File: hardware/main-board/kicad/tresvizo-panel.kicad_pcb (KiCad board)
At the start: 4 copper layers, 82.8 x 79 mm, 137 parts, among them J101 PANEL_USB, J102 BATTERY, J301 GNSS, J401 TF-015, J402 BOTON, J403 OLED, J404 NTC, J405 IMU, J501 USB_C, J502 PANEL_USB, Q101 AO3400A, Q102 AO3401A, Q103 AO3400A, Q401 AO3401A, Q402 AO3400A, SW201 RESET, SW202 BOOT, U101 USBLC6-2SC6, U102 BQ25798RQMR, U103 MAX17048G+T10, U105 TPS62903RPJR, U201 ESP32-S3-WROOM-1-N16R2, U301 TPS63070RNMR, U302 USBLC6-2SC6, U303 USBLC6-2SC6, U501 USBLC6-2SC6

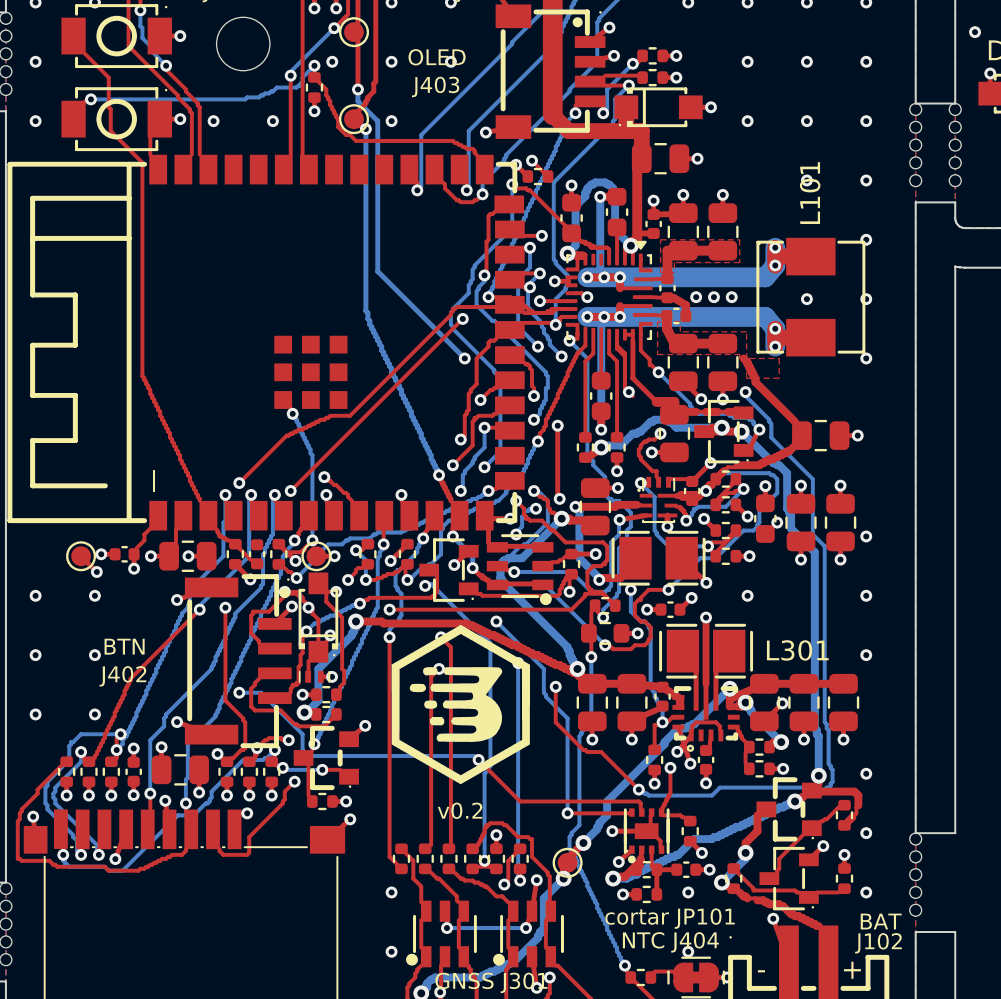
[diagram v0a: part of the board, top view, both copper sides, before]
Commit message: Placa principal v0.2: regulador de 3.3 V (TPS62903) colocado según su hoja de datos
- U105 y sus piezas pasan a la zona libre de la derecha de la placa.
- SW a L102 en 0.9 mm por F.Cu y sin vías. Antes daba un rodeo de 8.7 mm con dos vías y pasaba
  entre los pads de C115.
- C115, el 10 µF de entrada, queda a 0.4 mm de VIN y de GND, con EN saliendo entre sus pads.
- C118 y C119 (salida) junto a la salida de L102 y a GND; VOS toma la tensión en C118.
- FB con su divisor a 1.5 mm: 2.5 mm de pista sin vías (antes 8.6 mm con dos vías).
- Fuera los prerruteos de BUCK_SW y de la vía de GND de U105, que ya no hacen falta.
- ERC 0. DRC con 0 violaciones, 0 sin conectar y 0 de paridad en la placa, la panel-usb y el panel;
  128 de 128 conexiones; dos builds idénticos. Montaje en V2.3 sin choques nuevos.
- README: D+/D- con las cifras del ruteo actual (vienen de una revisión externa).
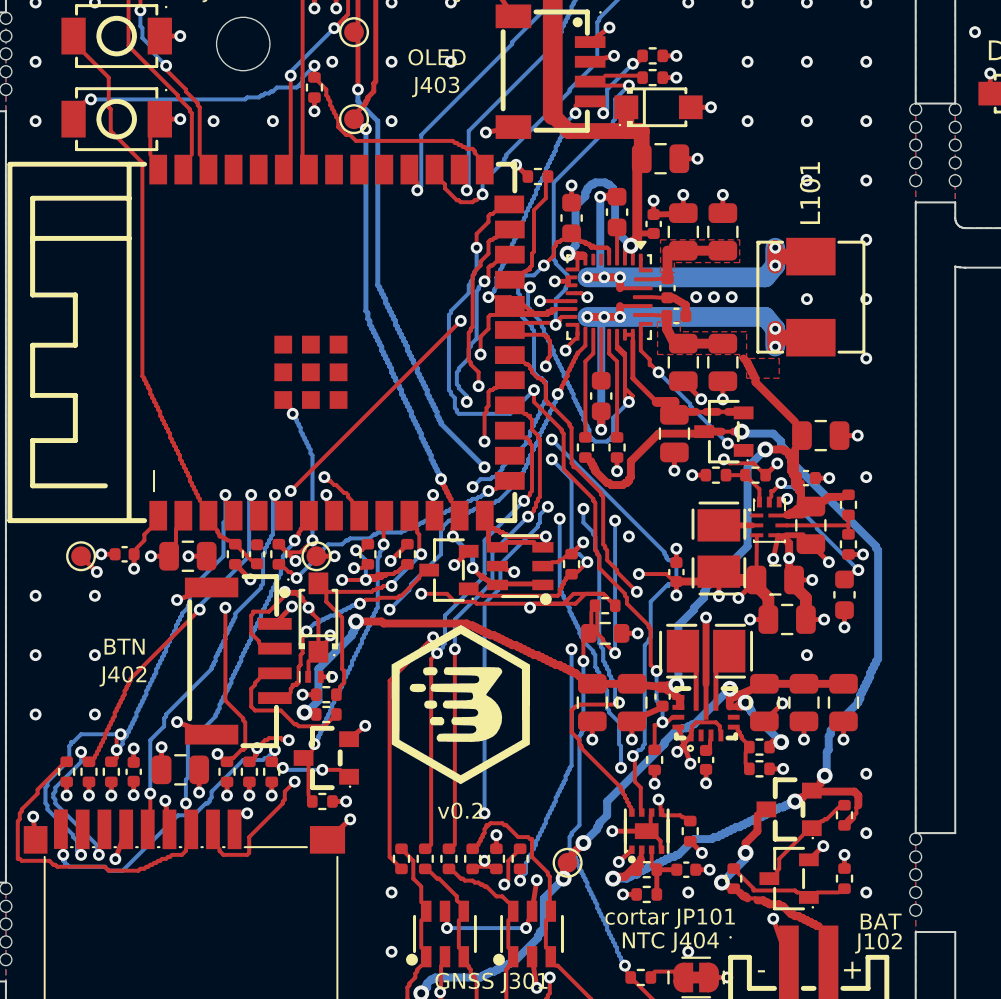
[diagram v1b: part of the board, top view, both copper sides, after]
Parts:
- moved C115 10.9 mm to (147.7, 140.9), turned to -90 degrees
- moved R116 6.51 mm to (149.6, 141.9), turned to -90 degrees
- moved R115 6.33 mm to (149.6, 139.9), turned to -90 degrees
- moved C116 5.79 mm to (147.4, 138.6), turned to 0 degrees
- moved U105 5.69 mm to (145.6, 140.6)
- moved C119 5.59 mm to (146.5, 145.7), turned to 0 degrees
- moved C117 5.55 mm to (149.4, 144.4), turned to -90 degrees
- moved R118 4.37 mm to (144.9, 138.4)
- moved C118 3.18 mm to (145.9, 143.7), turned to 0 degrees
- moved L102 3.09 mm to (143.1, 142.1), turned to -90 degrees
- moved R117 2.84 mm to (142.9, 138.4)
- moved C120 1.92 mm to (140.9, 143.3), turned to 90 degrees
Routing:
- net BTN_LED_EN: track 65.4 -> 25.6 mm, vias 5 -> 3
- net VSYS: track 91.1 -> 56.2 mm, vias 8 -> 4
- net I2C_SCL: track 77.8 -> 56.5 mm
- net GND: track 120.6 -> 130.6 mm, vias 155 -> 157
- net /Alimentación, carga y batería/BUCK_SW: track 8.68 -> 0.95 mm, vias 2 -> 0
- net /Alimentación, carga y batería/CHG_ILIM: track 22.7 -> 29.9 mm, vias 4 -> 5
- net /Alimentación, carga y batería/BUCK_FB: track 8.62 -> 2.47 mm, vias 2 -> 0
- net /Alimentación, carga y batería/REGN: track 53.3 -> 47.5 mm
- net /Alimentación, carga y batería/BUCK_EN: track 8.50 -> 4.13 mm, vias 2 -> 0
- net GNSS_PWR_EN: track 33.7 -> 38.0 mm
- net /Alimentación, carga y batería/BUCK_SS: track 11.4 -> 7.62 mm
- net +3V3: track 44.8 -> 47.6 mm
- net /Alimentación, carga y batería/VPACK: track 48.0 -> 50.6 mm, vias 6 -> 4
- net CHG_TS: track 38.0 -> 40.6 mm, vias 4 -> 5
- net GNSS_RESET_MCU: track 29.4 -> 31.9 mm, vias 5 -> 3
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
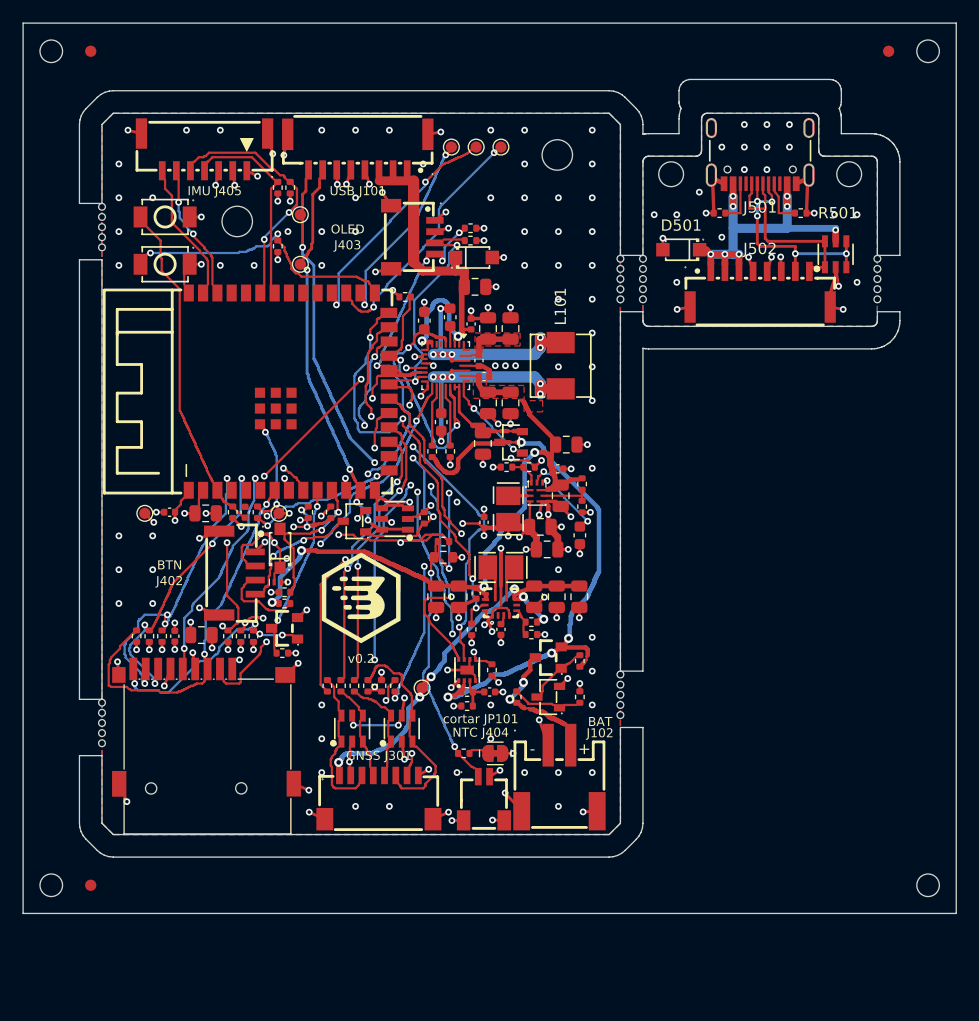
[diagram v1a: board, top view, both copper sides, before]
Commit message: Panel JLCPCB: fiduciales con el centro a 3.85 mm del canto
- JLCPCB pide fiduciales de 1 mm con el centro a 3.85 mm del canto del panel, para que no los tapen
  los rieles guía de la máquina. Estaban a 2.5 mm, en medio del riel de 5 mm.
- La abertura de máscara (Ø2) queda a 0.74 mm o más de la fresa, y los agujeros de herramienta, a
  2.75 mm.
- Las placas no cambian. DRC del panel con 0 violaciones; ERC 0 y DRC 0 en las dos placas.
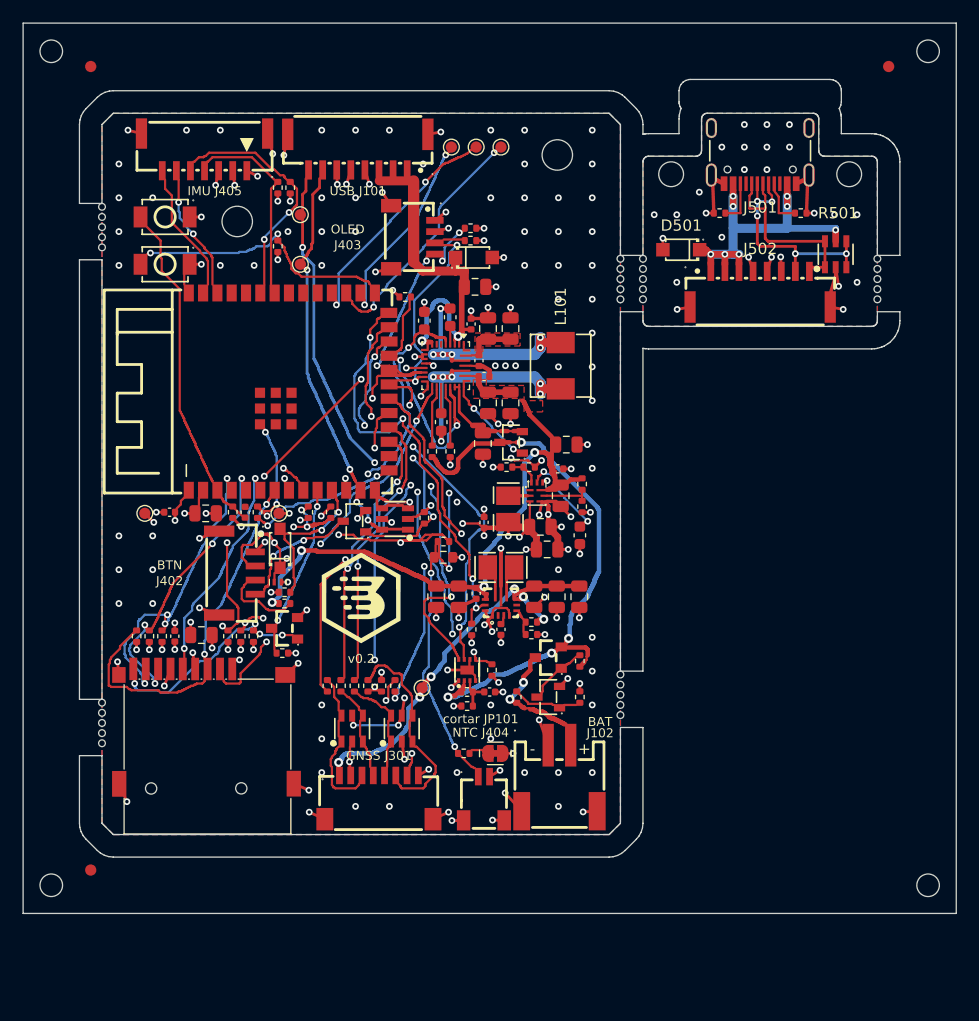
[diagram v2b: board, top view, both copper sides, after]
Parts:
- moved FID1 1.35 mm to (106.0, 102.8)
- moved FID2 1.35 mm to (176.8, 102.8)
- moved FID3 1.35 mm to (106.0, 174.2)

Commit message: Placa principal v0.2: NTC de la celda obligatoria en J404
- Fuera R106 (10k fijo) y el puente JP101: TS siempre ve la NTC. Sin NTC enchufada no carga;
  el sistema sigue encendido con el USB.
- Con el divisor 5.1k/30k y una NTC 10k B3435 (103AT), umbrales por omisión del BQ25798 (hoja
  de datos, VT1/TS_COOL/TS_WARM/VT5): no carga bajo ~2 ni sobre ~61 grados, 20 % de corriente
  entre ~2 y 11 y 400 mV menos de voltaje entre ~45 y 61.
- El número R106 queda reservado para no renumerar las demás resistencias.
- README: tabla de temperaturas, aviso de no usar NTC de 100k de impresora 3D y cómo va la NTC
  pegada a la celda en la carcasa V2.3.
- 126 de 126 conexiones; DRC 0, sin conectar 0 y paridad en la placa, la panel-usb y el panel;
  ERC 0. Costo estimado 209.08 USD por 5 juegos.
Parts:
- removed JP101: NTC_CORTAR, tresvizo_lcsc:SolderJumper-2_P1.3mm_Bridged_RoundedPad1.0x1.5mm
- removed R106: 10k, Resistor_SMD:R_0402_1005Metric
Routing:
- net /Alimentación, carga y batería/REGN: track 47.5 -> 41.2 mm, vias 5 -> 6
- net GNSS_PPS_MCU: track 24.0 -> 29.0 mm, vias 2 -> 5
- net GNSS_PWR_EN: track 38.0 -> 33.2 mm, vias 4 -> 3
- net USB_DP: track 37.6 -> 33.2 mm
- net BTN_LED_EN: track 25.6 -> 28.8 mm
- net CHG_INT_N: track 24.7 -> 27.4 mm, vias 2 -> 4
- net GNSS_RESET_MCU: track 31.9 -> 30.1 mm
- net GNSS_TXD2_MCU: track 22.9 -> 24.5 mm, vias 2 -> 3
- net I2C_SCL: track 56.5 -> 55.0 mm, vias 7 -> 8
- net +3V3: track 47.6 -> 48.9 mm
- net /Alimentación, carga y batería/VPACK: track 50.6 -> 51.9 mm
- net CHG_TS: track 40.6 -> 39.4 mm, vias 5 -> 4
- net GNSS_EVENT_MCU: track 27.9 -> 26.8 mm, vias 4 -> 3
- net /Alimentación, carga y batería/CHG_TS_FIJA: track 1.00 -> 0.00 mm
- net GND: track 130.6 -> 129.9 mm, vias 157 -> 155
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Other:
- board text removed: "cortar JP101"
